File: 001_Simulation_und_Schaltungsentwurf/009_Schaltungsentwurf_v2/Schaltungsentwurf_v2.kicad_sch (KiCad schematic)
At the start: 87 parts, among them IC1 MPY634KP, IC2 MPY634KP, IC3 MPY634KP, J1 Screw_Terminal_01x04, J2 Conn_Coaxial, J3 Conn_Coaxial, J4 Conn_Coaxial, J5 Conn_Coaxial, J6 Conn_Coaxial, SW2 SW_MEC_5G, U1 TL082, U2 TL082, U3 MCP4261-104E_P, U4 MCP4261-104E_P, U5 TL082, U6 LM2596T-3.3

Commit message: pcb_version_2, new pcb holder
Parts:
- removed R10, R11: 1k, 000_OUF:Resistor, symbol Device:R_Small
- removed TP14: ZCD, 000_OUF:TestPoint, symbol 000_My_Symbols:Testpoint
- added D1: D_Zener, 000_OUF:1N4001, symbol Device:D_Zener
- added D2: D_Schottky, 000_OUF:1N4001, symbol Device:D_Schottky
- added JP12: Jumper3, 000_OUF:Connector 3 Pin 2,54mm, symbol Jumper:Jumper_3_Bridged12
- added JP15: RV6.1, 000_OUF:Connector 2 Pin 2.54mm, symbol Jumper:Jumper_2_Small_Open
- added JP17: PD_out, 000_OUF:Connector 2 Pin 2.54mm, symbol Jumper:Jumper_2_Small_Open
- added JP18: RV7.2, 000_OUF:Connector 2 Pin 2.54mm, symbol Jumper:Jumper_2_Small_Open
- added R7: 10k, 000_OUF:Resistor, symbol Device:R_Small
- added R8: 1.2k, 000_OUF:Resistor, symbol Device:R_Small
- added RV6, RV7: 10k, Potentiometer_THT:Potentiometer_Bourns_3296Y_Vertical, symbol Device:R_Potentiometer
- added TP16: Vc_DC+, 000_OUF:TestPoint, symbol 000_My_Symbols:Testpoint
- added TP17: Vc_DC-, 000_OUF:TestPoint, symbol 000_My_Symbols:Testpoint
- added TP7, TP9: Backup, 000_OUF:TestPoint, symbol 000_My_Symbols:Testpoint
- C1: footprint 000_OUF:1-10uF -> 000_OUF:100nF
- C6: renamed from C3; footprint 000_OUF:1-10uF -> 000_OUF:100nF
- C9: renamed from C5; footprint 000_OUF:1-10uF -> 000_OUF:100nF
- JP13: renamed from JP14; value R2_out -> PD_in
- JP14: renamed from JP12; value Jumper3 -> RV7.1
- L1: footprint Inductor_THT:L_Radial_D12.0mm_P5.00mm_Fastron_11P -> Inductor_THT:L_Radial_D8.7mm_P5.00mm_Fastron_07HCP
- R9: renamed from R7; value 1k -> 100k
- SW1: renamed from SW2; footprint (none) -> Button_Switch_THT:SW_DIP_SPSTx03_Piano_10.8x9.18mm_W7.62mm_P2.54mm
- TP8: value Vc_DC -> Backup
- renumbered C6 to C10, C7 to C11, C8 to C12, C9 to C13, C10 to C14, C11 to C2, C12 to C3, C13 to C4, C2 to C5, C14 to C7, C4 to C8, D1 to D3, JP13 to JP19, R9 to R10, R8 to R11, TP4 to TP10, TP5 to TP11, TP7 to TP12, TP15 to TP13, TP6 to TP14, TP9 to TP18, TP16 to TP2, TP10 to TP20, TP20 to TP21, TP11 to TP22, TP12 to TP23, TP13 to TP24, TP17 to TP3, TP18 to TP4, TP2 to TP5, TP3 to TP6
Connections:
- net GND: now also D1.2 (A), R7.1
- net HPF: no longer IC1.1 (X_1_INPUT), JP13.2 (B)
- net Vc: now also JP17.2 (B), JP18.2 (B)
- net ZCD: now also JP12.1 (A); no longer R9.2, U5.7
- net at JP14.1 (A), RV5.2: now also TP17.1
- net at JP14.2 (C): now also RV7.2, RV7.3; no longer TP8.1
- net at JP14.3 (B), RV4.2: now also TP16.1
- net at A1.14 (GPIO10): now also TP7.1
- net at A1.15 (GPIO11): now also TP8.1
- net at A1.16 (GPIO12): now also TP9.1
- net at A1.27 (GPIO21): now also JP12.3 (B)
- net at C9.2, U5.1: now also JP15.1 (A)
- new net: JP18.1 (A), RV7.1
- new net: JP17.1 (A), RV6.1
- new net: R8.1, R9.2, U5.7
- new net: D2.2 (A), R8.2
- new net: JP15.2 (B), RV6.2, RV6.3
- new net: D1.1 (K), D2.1 (K), JP12.2 (C), R7.2
- new net HPF_in: IC1.1 (X_1_INPUT), JP13.2 (B)
- no-connect marks 16 -> 18
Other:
- note removed: "*Mehr TP überall/ Jumper *Vier DigitalPots für die vier widerstände *Überlegungen für ADC und VCO *RP muss hinzugefügt werden *3.3V Spannuungsversorgung für RP"
- moved on the sheet: C9, JP13, JP14, R10, R11, R5, R9, RV4, RV5, TP12, TP13, TP20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

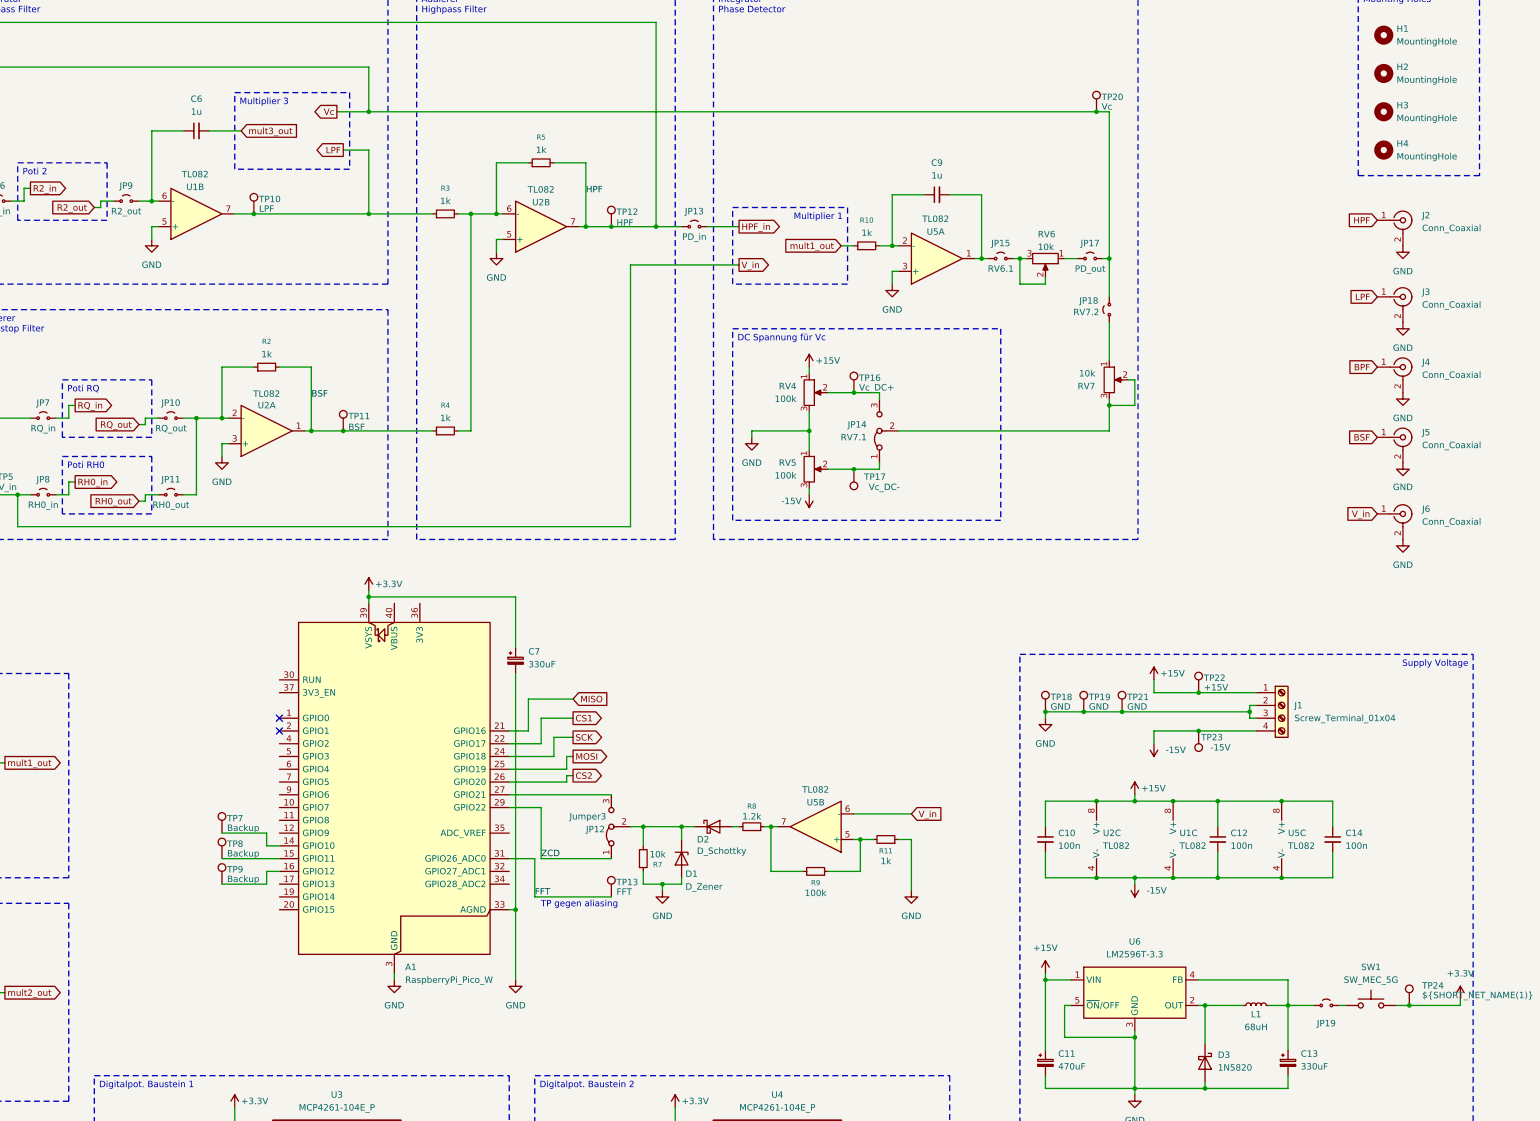
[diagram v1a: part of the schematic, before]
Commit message: PD-Vermessung und Sprungantwortsimulation
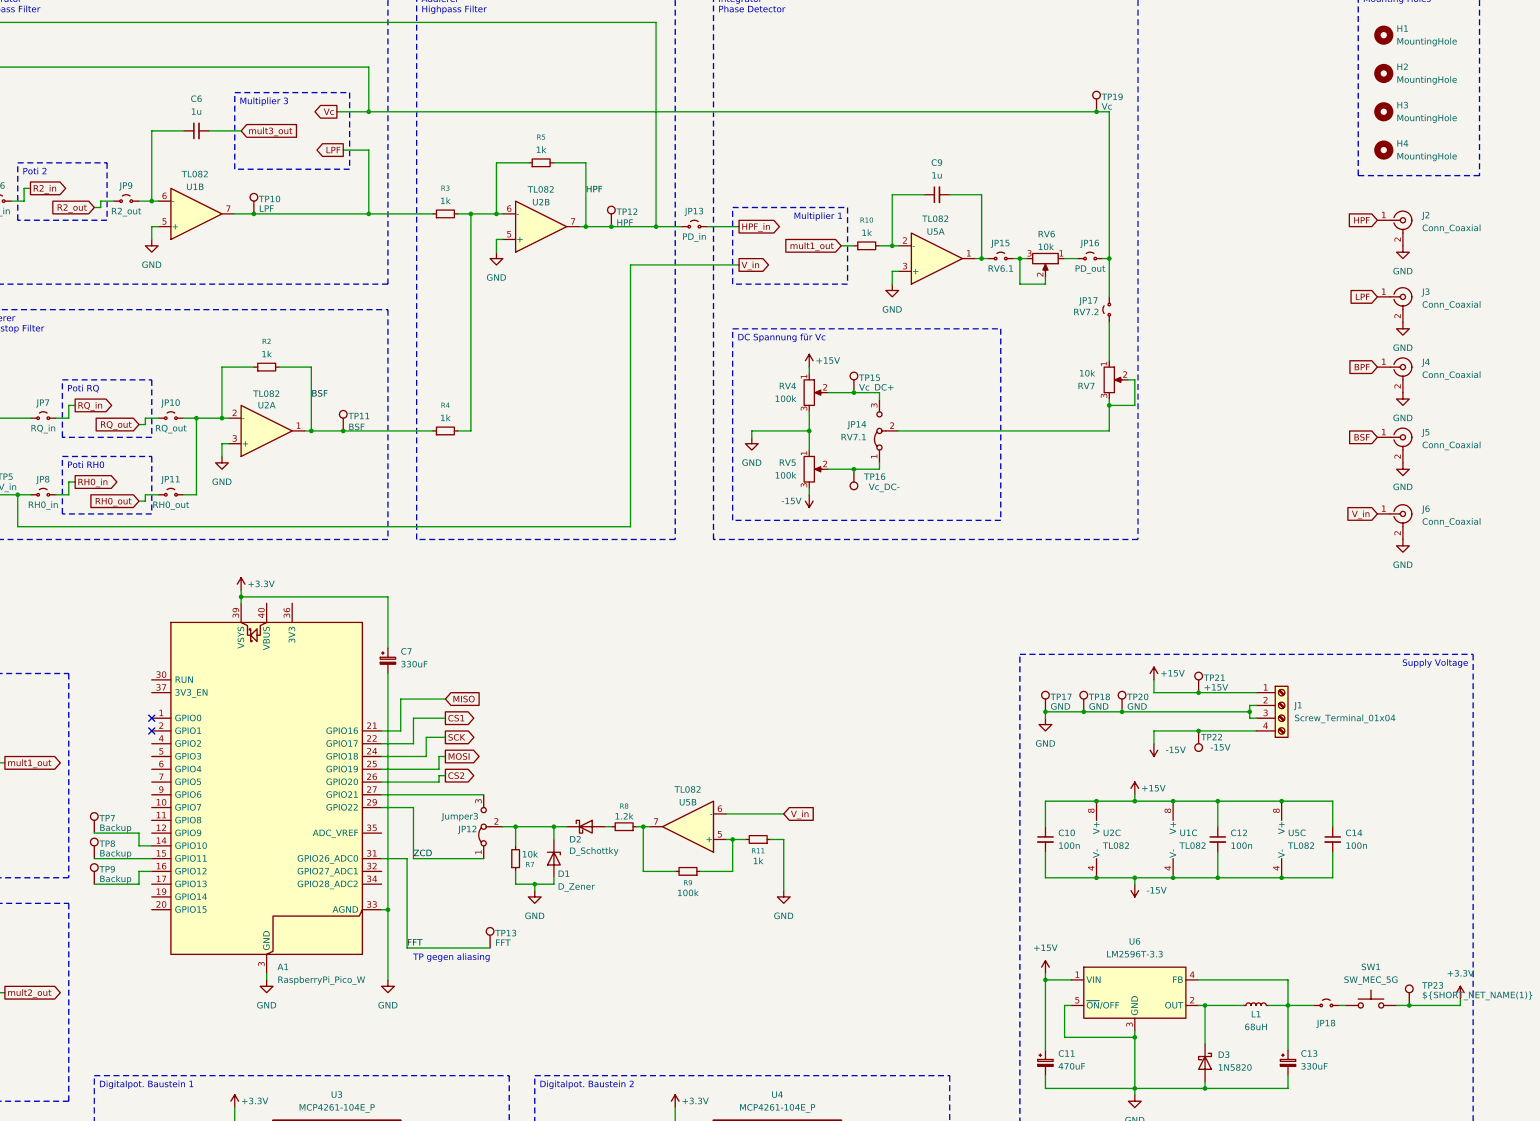
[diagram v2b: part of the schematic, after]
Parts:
- renumbered JP17 to JP16, JP18 to JP17, JP19 to JP18, TP16 to TP15, TP17 to TP16, TP18 to TP17, TP19 to TP18, TP20 to TP19, TP21 to TP20, TP22 to TP21, TP23 to TP22, TP24 to TP23
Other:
- moved on the sheet: A1, C7, D1, D2, JP12, R11, R7, R8, R9, TP13, TP7, TP8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

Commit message: aktueller Stand
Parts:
- C9: value 1u -> 100n
- R10: value 1k -> 100
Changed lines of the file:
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@@
 			)
 		)
-		(property "Value" "1k"
+		(property "Value" "100"
 			(at 281.94 64.77 90)
 			(effects
@@
 			)
 		)
-		(property "Value" "1u"
+		(property "Value" "100n"
 			(at 295.9163 53.34 90)
 			(effects

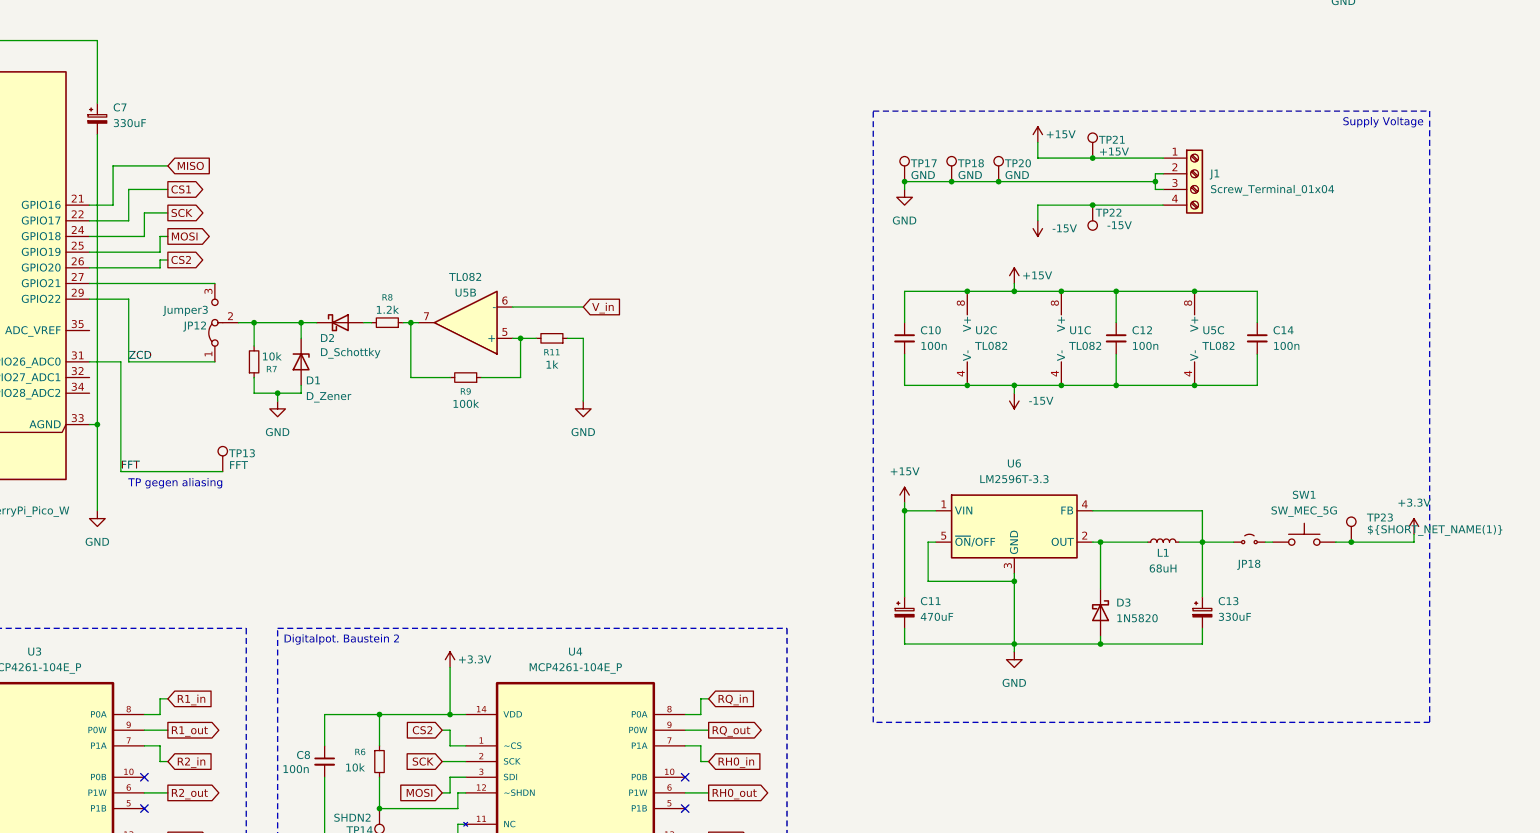
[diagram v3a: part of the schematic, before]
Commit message: Hinzufügen der PDF
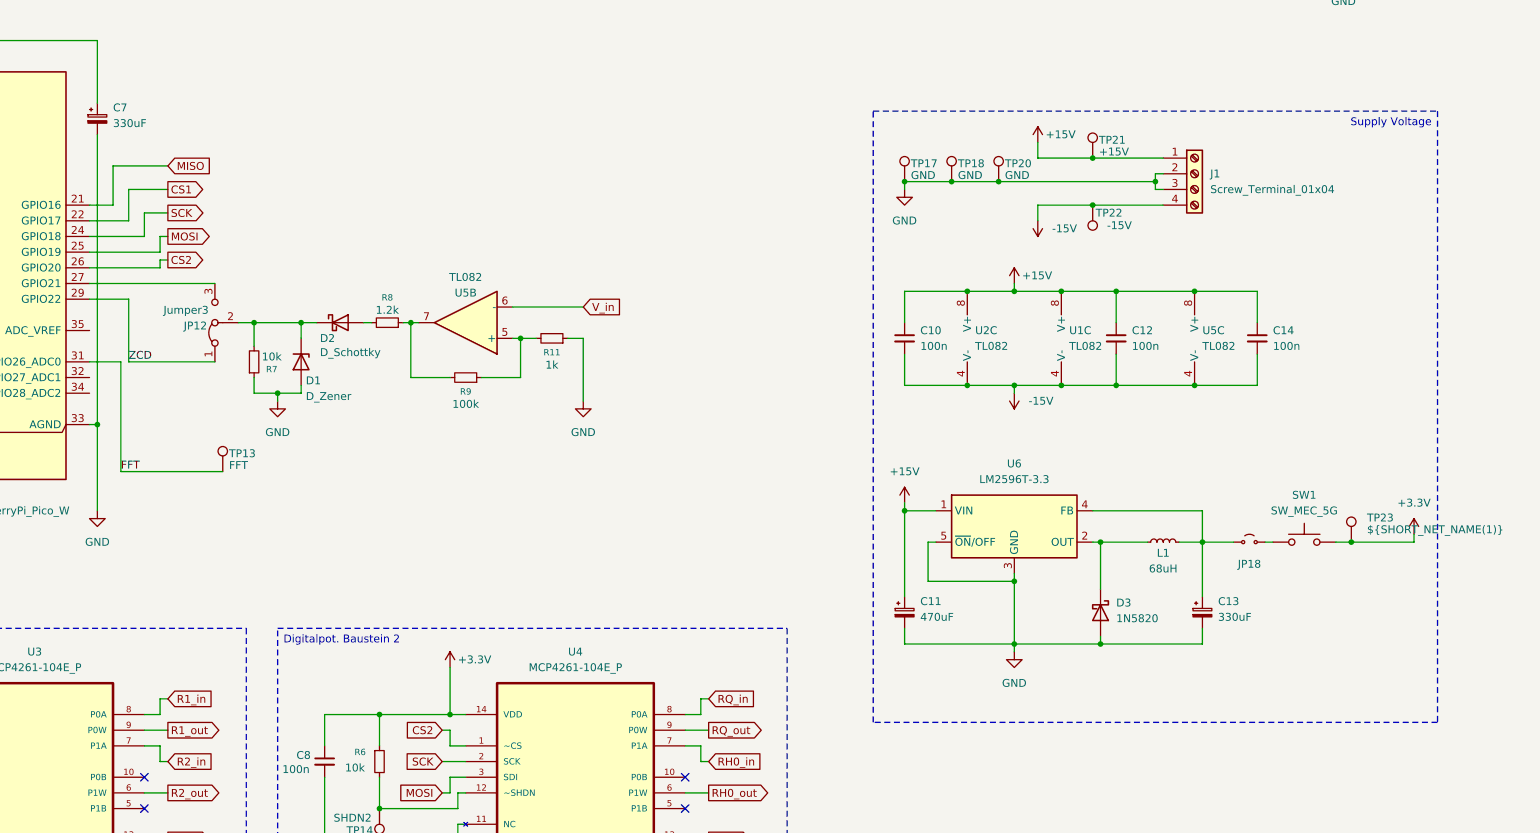
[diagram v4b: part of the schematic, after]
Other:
- note removed: "TP gegen aliasing"
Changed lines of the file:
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@@
 	(generator_version "9.0")
 	(paper "A3")
-	(text "TP gegen aliasing"
-		(exclude_from_sim no)
-		(at 199.39 209.042 0)
-		(effects
-			(font
-				(size 1.27 1.27)
-			)
-		)
-	)
 	(text_box "Poti 2\n\n"
 		(exclude_from_sim no)
@@
 		(exclude_from_sim yes)
 		(at 312.42 148.59 0)
-		(size 90.17 99.06)
+		(size 91.44 99.06)
 		(margins 0.9525 0.9525 0.9525 0.9525)
 		(stroke
@@
 		(at 107.95 116.84 0)
 		(unit 1)
-		(exclude_from_sim yes)
+		(exclude_from_sim no)
 		(in_bom yes)
 		(on_board yes)
@@
 		(at 128.27 184.15 0)
 		(unit 1)
-		(exclude_from_sim yes)
+		(exclude_from_sim no)
 		(in_bom yes)
 		(on_board yes)
@@
 		(at 144.78 261.62 180)
 		(unit 1)
-		(exclude_from_sim yes)
+		(exclude_from_sim no)
 		(in_bom yes)
 		(on_board yes)
@@
 		(at 207.01 207.01 0)
 		(unit 1)
-		(exclude_from_sim yes)
+		(exclude_from_sim no)
 		(in_bom yes)
 		(on_board yes)
@@
 		(at 279.4 96.52 0)
 		(unit 1)
-		(exclude_from_sim yes)
+		(exclude_from_sim no)
 		(in_bom yes)
 		(on_board yes)
@@
 		(at 327.66 40.64 0)
 		(unit 1)
-		(exclude_from_sim yes)
+		(exclude_from_sim no)
 		(in_bom yes)
 		(on_board yes)
@@
 		(at 389.89 218.44 0)
 		(unit 1)
-		(exclude_from_sim yes)
+		(exclude_from_sim no)
 		(in_bom no)
 		(on_board yes)
@@
 		(at 231.14 63.5 0)
 		(unit 1)
-		(exclude_from_sim yes)
+		(exclude_from_sim no)
 		(in_bom yes)
 		(on_board yes)
@@
 		(at 72.39 58.42 0)
 		(unit 1)
-		(exclude_from_sim yes)
+		(exclude_from_sim no)
 		(in_bom yes)
 		(on_board yes)
@@
 		(at 160.02 60.96 0)
 		(unit 1)
-		(exclude_from_sim yes)
+		(exclude_from_sim no)
 		(in_bom yes)
 		(on_board yes)
@@
 		(at 128.27 189.23 0)
 		(unit 1)
-		(exclude_from_sim yes)
+		(exclude_from_sim no)
 		(in_bom yes)
 		(on_board yes)
@@
 		(at 279.4 111.76 180)
 		(unit 1)
-		(exclude_from_sim yes)
+		(exclude_from_sim no)
 		(in_bom yes)
 		(on_board yes)
@@
 		(at 99.06 170.18 0)
 		(unit 1)
-		(exclude_from_sim yes)
+		(exclude_from_sim no)
 		(in_bom yes)
 		(on_board yes)
@@
 		(at 177.8 104.14 0)
 		(unit 1)
-		(exclude_from_sim yes)
+		(exclude_from_sim no)
 		(in_bom yes)
 		(on_board yes)
@@
 		(at 128.27 194.31 0)
 		(unit 1)
-		(exclude_from_sim yes)
+		(exclude_from_sim no)
 		(in_bom yes)
 		(on_board yes)
